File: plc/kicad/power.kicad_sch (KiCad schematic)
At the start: 85 parts, among them Q5 BSS138LT1G, Q6 CSD19537Q3, SW3 TSD003B08026A03, U14 LMR16006XDDCR, U15 TPS7A5201QRGRRQ1, U16 TPS26630RGER, U21 TPS54560BDDAR

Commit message: TPS7A52-Q1 PCB placement
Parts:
- C37: value 10u -> 22u
- C39: LCSC Part (none) -> C86295
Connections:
- net 5V is gone; now on net +5V: C32.2, C34.2, C35.2, C37.2, D9.2 (A), L4.2, R75.1, TP21.1, U15.14 (EN), U15.15 (IN), U15.16 (IN), U15.17 (IN)
- net +5V: no longer D10.1 (C), D11.1 (C)
- new net ++5V: D10.1 (C), D11.1 (C)
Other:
- note added: "+5V, 5A"
- note removed: "5V, 5A"
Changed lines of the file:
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@@
 		)
 	)
-	(text "5V, 5A"
+	(text "+5V, 5A"
 		(exclude_from_sim no)
 		(at 169.545 38.735 0)
@@
 			)
 		)
+		(property "LCSC Part" "C86295"
+			(at 355.6 202.565 0)
+			(hide yes)
+			(show_name no)
+			(do_not_autoplace no)
+			(effects
+				(font
+					(size 1.27 1.27)
+				)
+			)
+		)
 		(pin "2"
 		)
@@
 			)
 		)
-		(property "Value" "5V"
+		(property "Value" "+5V"
 			(at 329.565 205.7399 90)
 			(show_name no)
@@
 			)
 		)
-		(property "Value" "5V"
+		(property "Value" "+5V"
 			(at 173.99 33.02 0)
 			(show_name no)
@@
 			)
 		)
-		(property "Value" "+5V"
+		(property "Value" "++5V"
 			(at 255.905 60.325 0)
 			(show_name no)
@@
 			)
 		)
-		(property "Value" "5V"
+		(property "Value" "+5V"
 			(at 382.905 215.265 0)
 			(show_name no)
@@
 			)
 		)
-		(property "Value" "10u"
+		(property "Value" "22u"
 			(at 379.73 226.6949 0)
 			(show_name no)
@@
 			)
 		)
-		(property "Value" "5V"
+		(property "Value" "+5V"
 			(at 147.32 81.9149 90)
 			(show_name no)

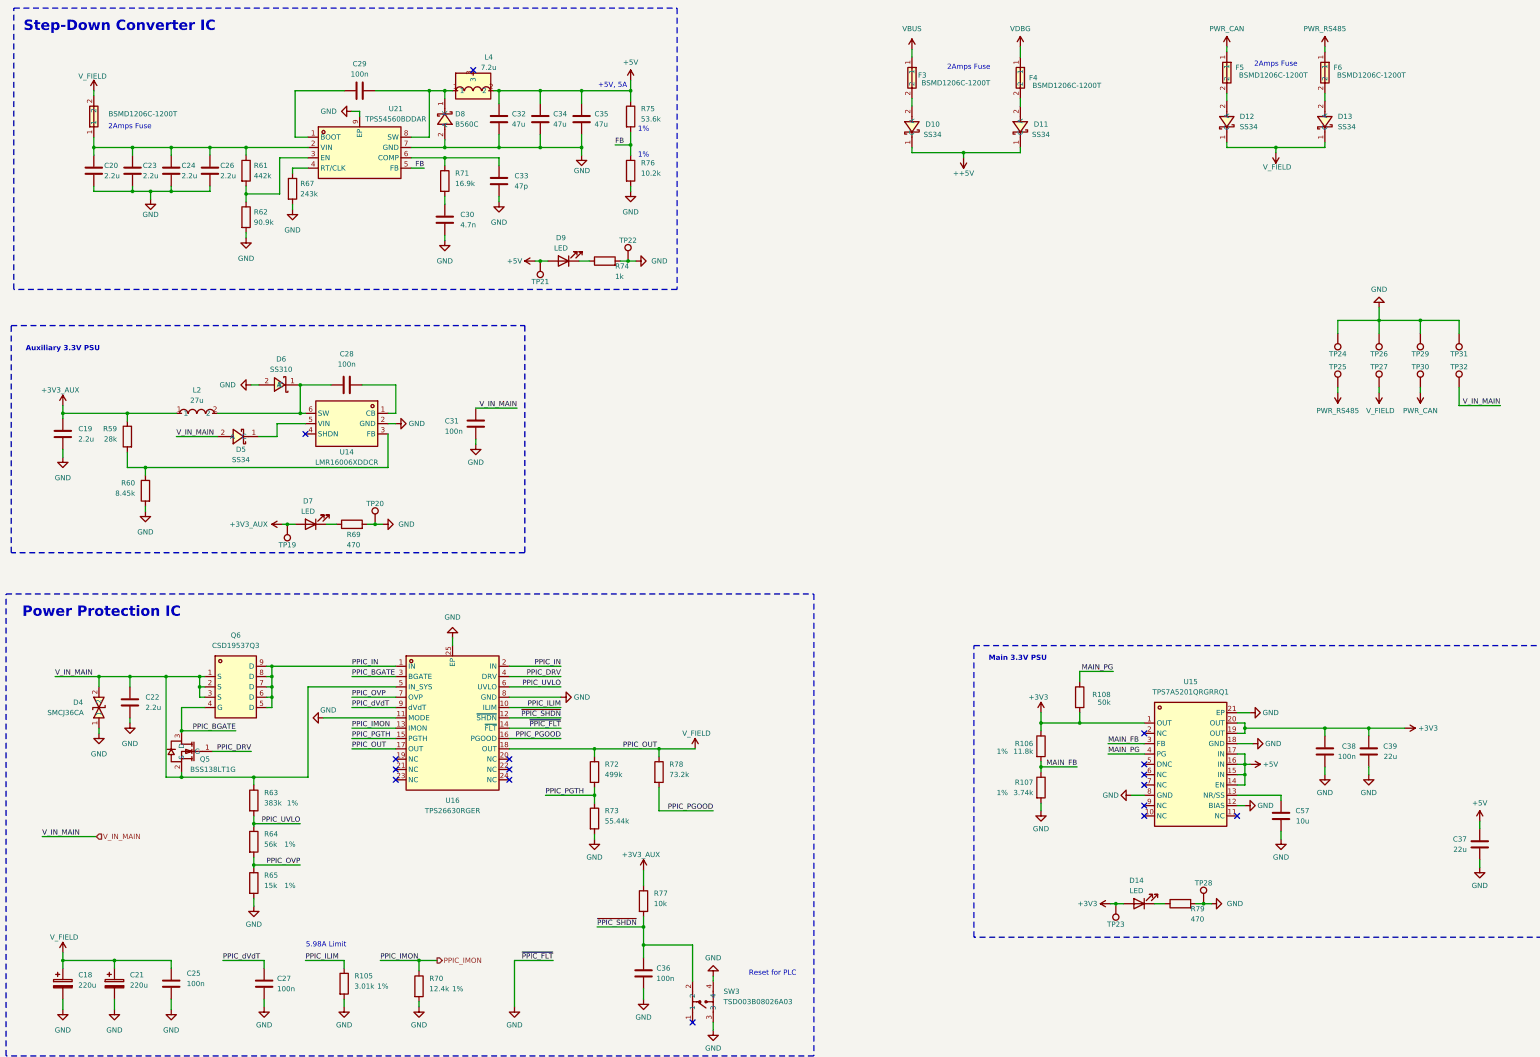
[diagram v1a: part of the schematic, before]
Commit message: Rearranged small PCB placements
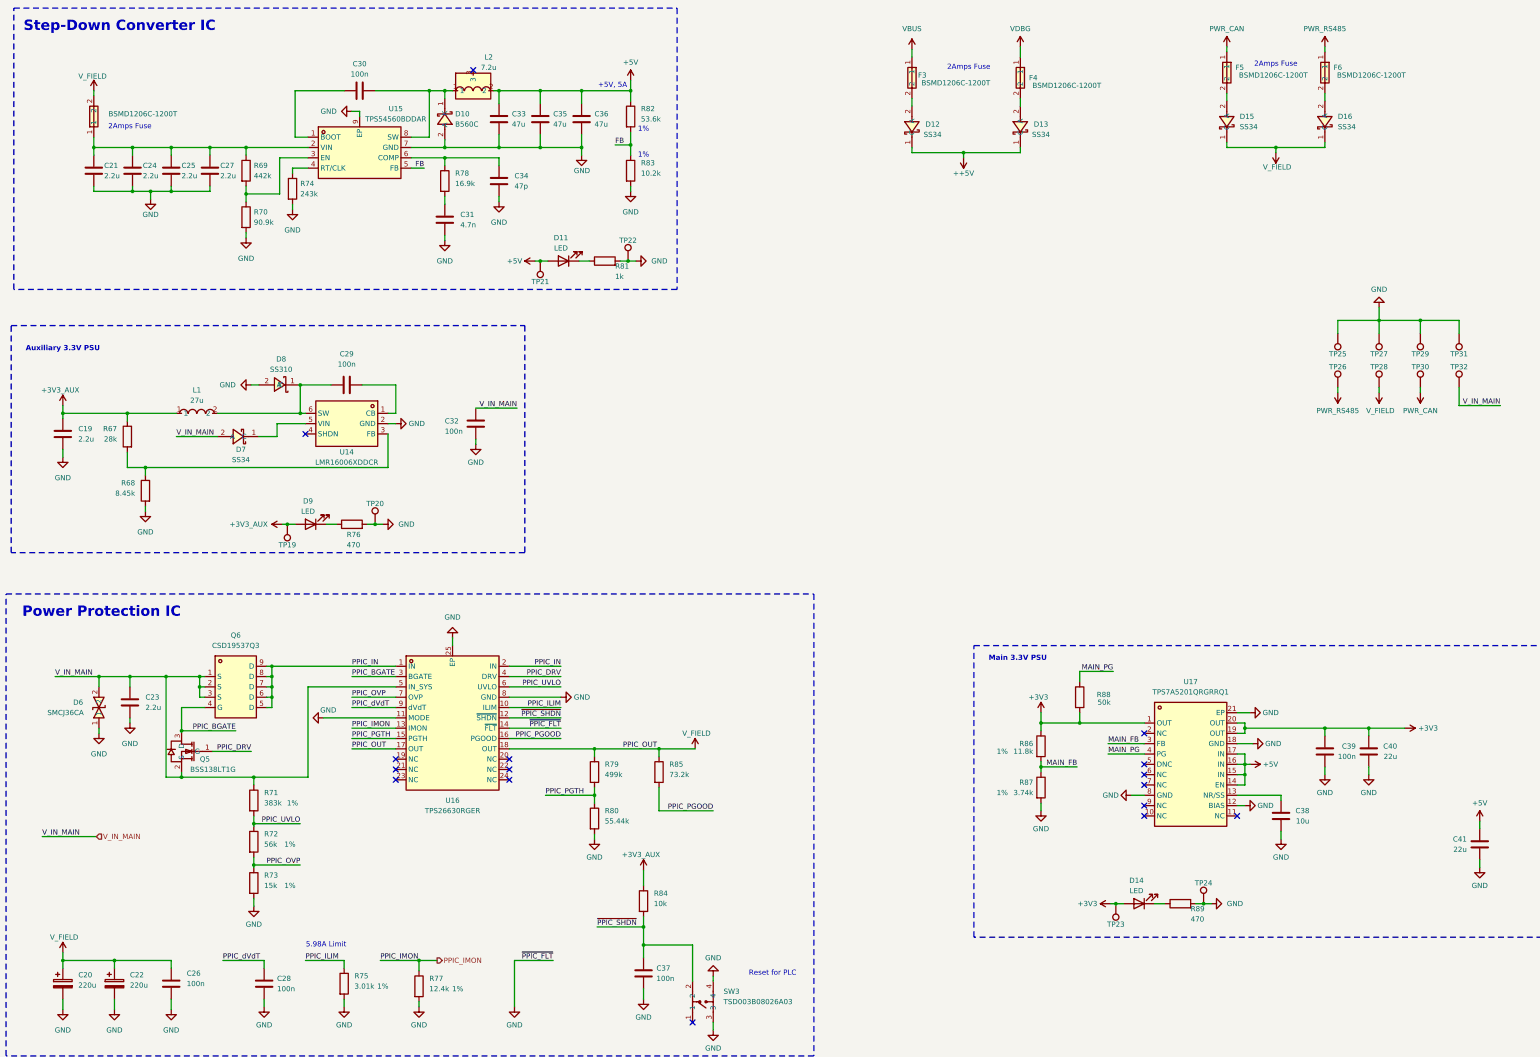
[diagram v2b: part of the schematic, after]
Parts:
- renumbered C18 to C20, C20 to C21, C21 to C22, C22 to C23, C23 to C24, C24 to C25, C25 to C26, C26 to C27, C27 to C28, C28 to C29, C29 to C30, C30 to C31, C31 to C32, C32 to C33, C33 to C34, C34 to C35, C35 to C36, C36 to C37, C57 to C38, C38 to C39, C39 to C40, C37 to C41, D8 to D10, D9 to D11, D10 to D12, D11 to D13, D12 to D15, D13 to D16, D4 to D6, D5 to D7, D6 to D8, D7 to D9, L2 to L1, L4 to L2, R59 to R67, R60 to R68, R61 to R69, R62 to R70, R63 to R71, R64 to R72, R65 to R73, R67 to R74, R105 to R75, R69 to R76, R70 to R77, R71 to R78, R72 to R79, R73 to R80, R74 to R81, R75 to R82, R76 to R83, R77 to R84, R78 to R85, R106 to R86, R107 to R87, R108 to R88, R79 to R89, TP28 to TP24, TP24 to TP25, TP25 to TP26, TP26 to TP27, TP27 to TP28, U21 to U15, U15 to U17

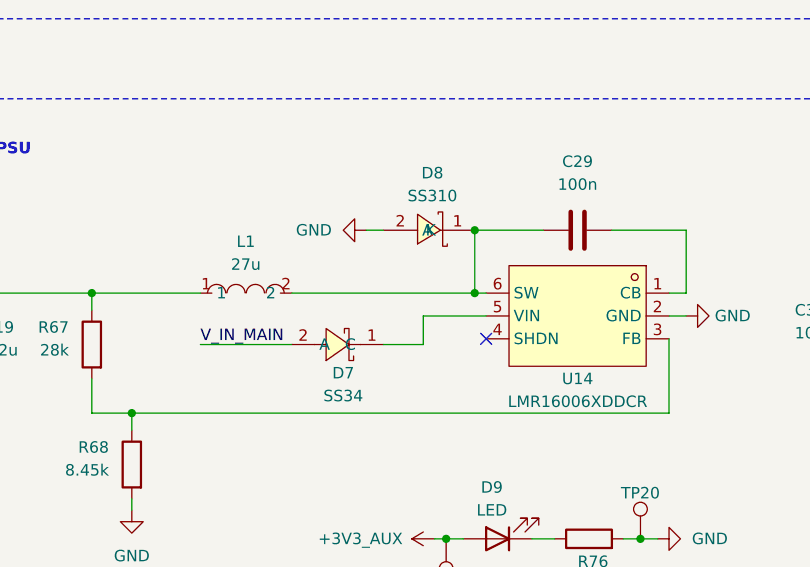
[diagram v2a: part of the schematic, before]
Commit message: Updated PCB placement
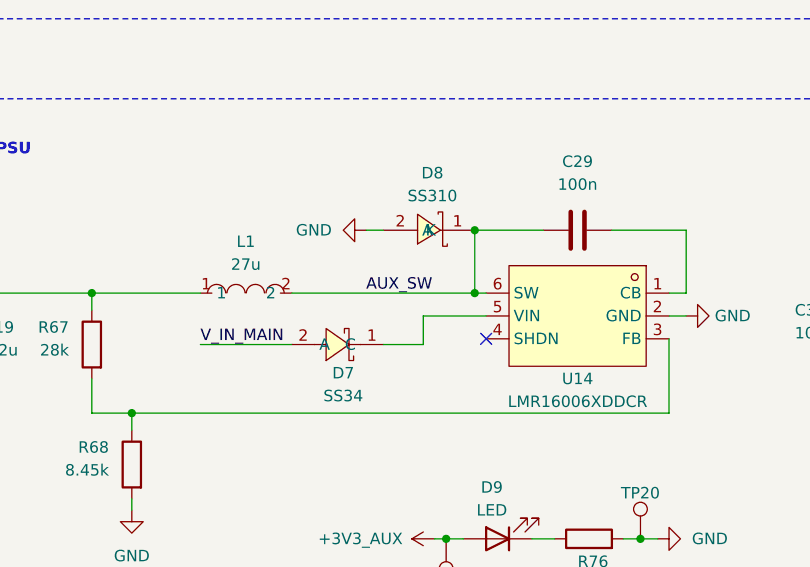
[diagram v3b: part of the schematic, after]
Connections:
- net AUX_SW: now reaches C29.2, D8.1 (K), L1.2, U14.6 (SW)
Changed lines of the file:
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@@
+		)
+	)
+	(label "AUX_SW"
+		(at 80.645 119.38 0)
+		(effects
+			(font
+				(size 1.27 1.27)
+			)
+			(justify left bottom)
 		)
 	)

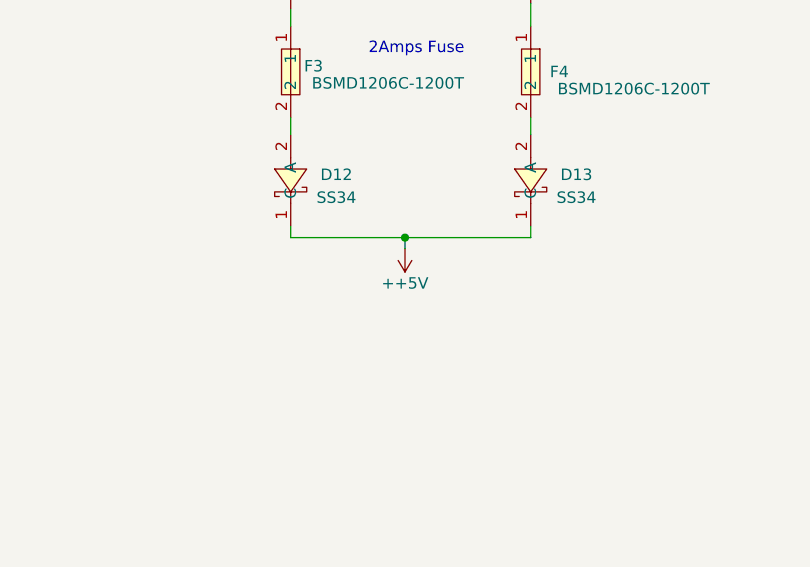
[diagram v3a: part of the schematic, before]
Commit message: Added mounting holes & PCB outline
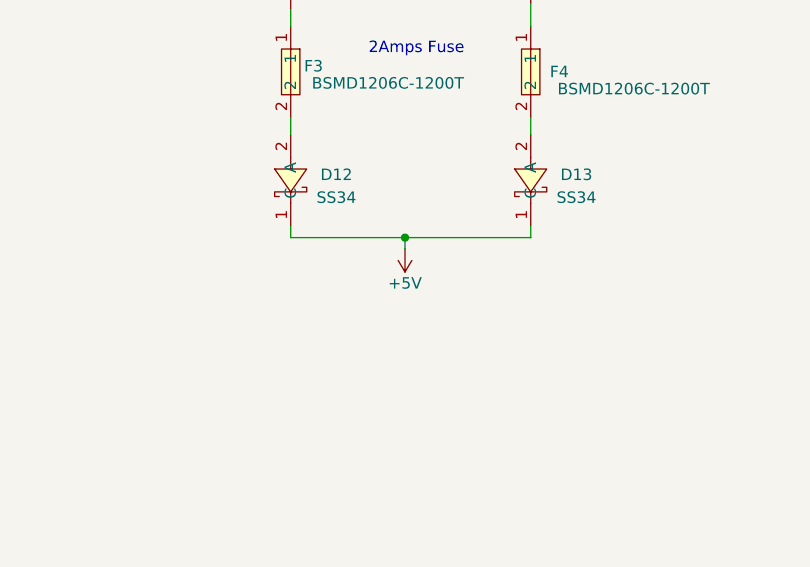
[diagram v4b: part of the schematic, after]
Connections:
- net ++5V is gone; now on net +5V: D12.1 (C), D13.1 (C)
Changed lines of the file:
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@@
 			)
 		)
-		(property "Value" "++5V"
+		(property "Value" "+5V"
 			(at 255.905 60.325 0)
 			(show_name no)

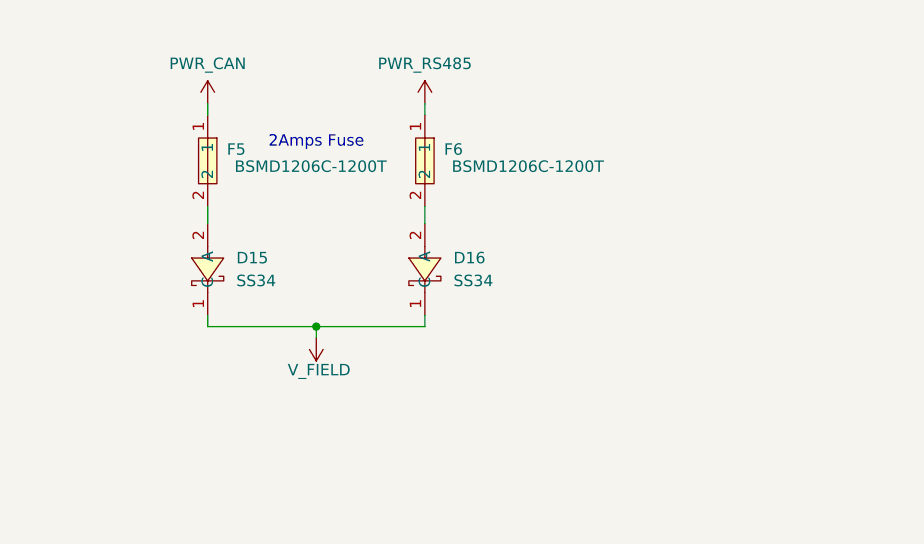
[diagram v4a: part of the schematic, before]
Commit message: Changed CAN & RS485 to input voltage unprotected
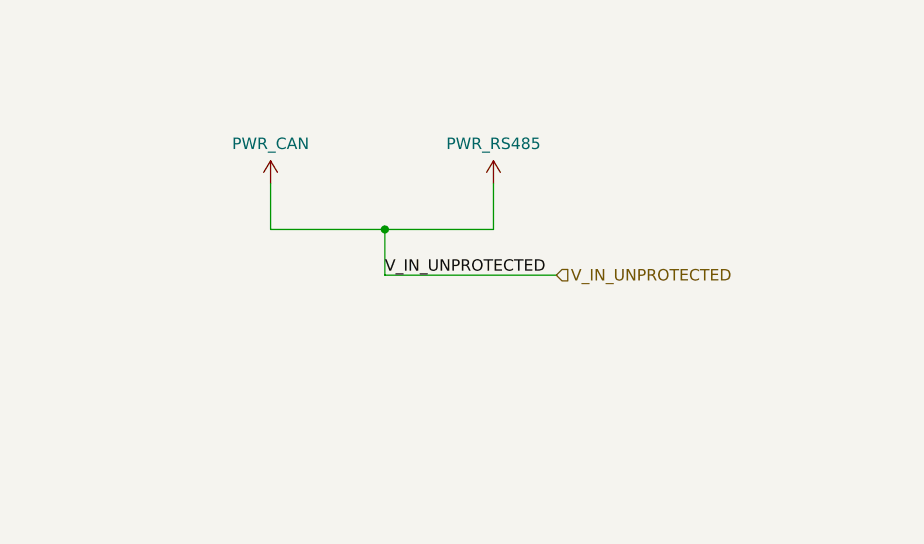
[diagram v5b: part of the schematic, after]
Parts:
- removed D15, D16: SS34, LibrePLC32:SMA_L4.3-W2.7-LS5.1-RD, symbol LibrePLC32:SS34_C908680
- removed F5, F6: BSMD1206C-1200T, LibrePLC32:F1206, symbol LibrePLC32:BSMD1206C-1200T
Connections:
- net PWR_RS485 is gone; now on net PWR_CAN: TP26.1
